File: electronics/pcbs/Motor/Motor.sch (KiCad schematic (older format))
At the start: 17 parts, among them J1 Left Encoder, J2 Right Encoder, J3 Battery, J4 I2C, P1 Digital, P10 CONN_01X01, P11 CONN_01X01, P12 CONN_01X01, P13 CONN_01X01, P2 Power, P3 Analog, P4 Analog, P5 PWM, P6 PWM, P7 Communication, P8 CONN_01X01, P9 CONN_01X01

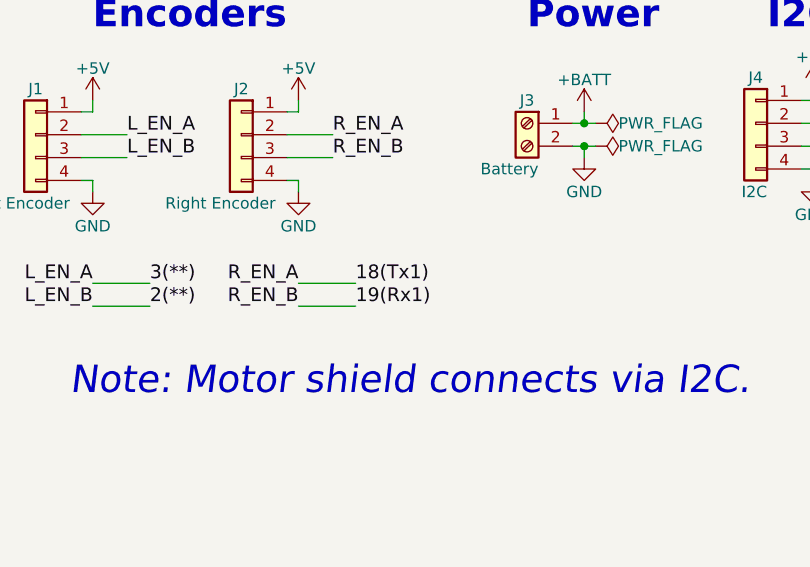
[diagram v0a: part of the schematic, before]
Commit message: Motor PCB: Redesigned PCB. Swapped pins for Encoder R's A and B so that layout was easier.
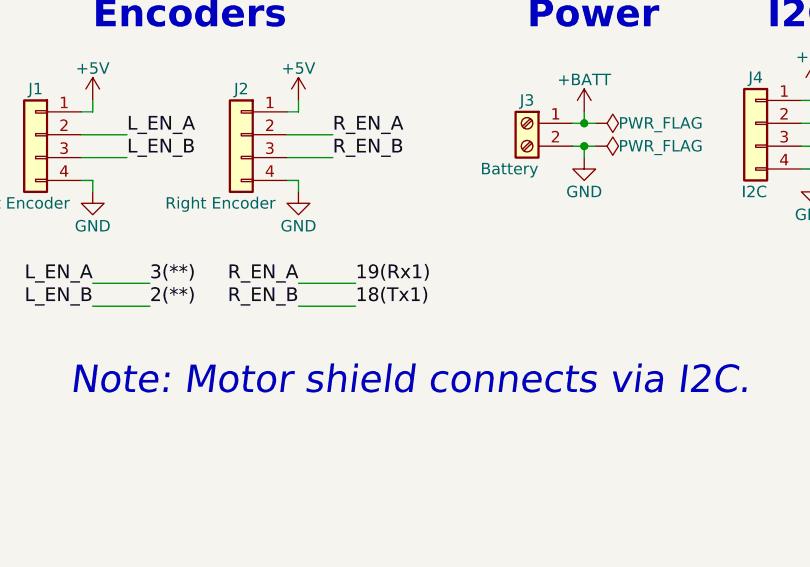
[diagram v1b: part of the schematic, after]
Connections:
- net 18(Tx1): now also J2.3 (Pin_3); no longer J2.2 (Pin_2)
- net 19(Rx1): now also J2.2 (Pin_2); no longer J2.3 (Pin_3)
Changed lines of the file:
@@
 Text Label 3950 2300 0    60   ~ 0
 3(**)
+Text Label 4850 2400 0    60   ~ 0
+18(Tx1)
 Text Label 4850 2300 0    60   ~ 0
-18(Tx1)
-Text Label 4850 2400 0    60   ~ 0
 19(Rx1)
 Wire Wire Line

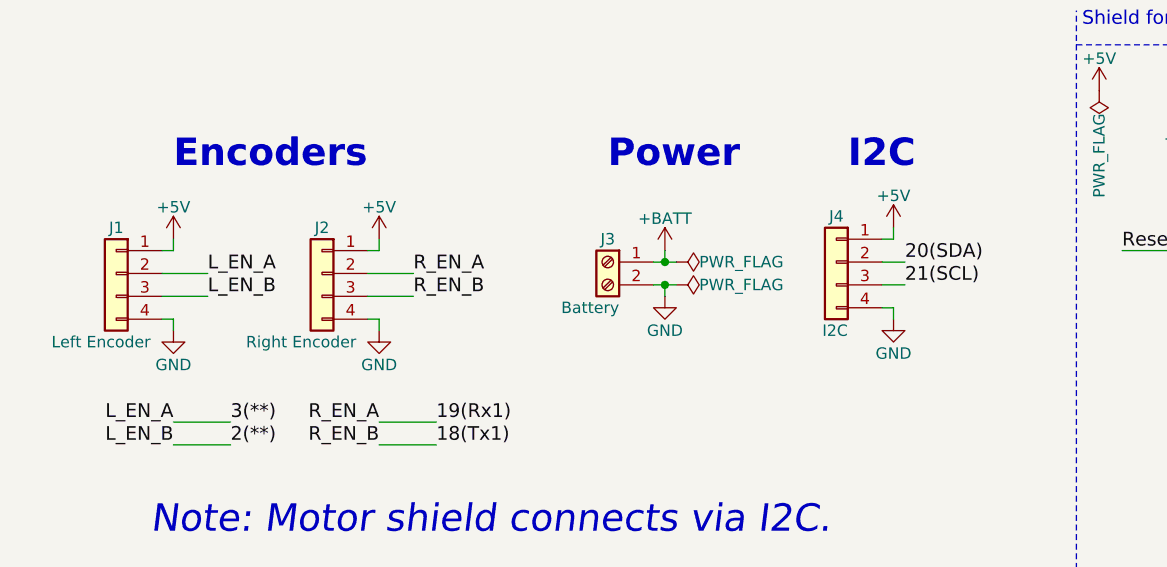
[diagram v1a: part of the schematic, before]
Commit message: Primary/Motor PCBs: Rearranged the GND pin on breakout headers so that we can avoid needing two layers. This change makes the boards more easily prototyped using hobbyist tools like the OtherMill, where plating holes and vias is difficult.
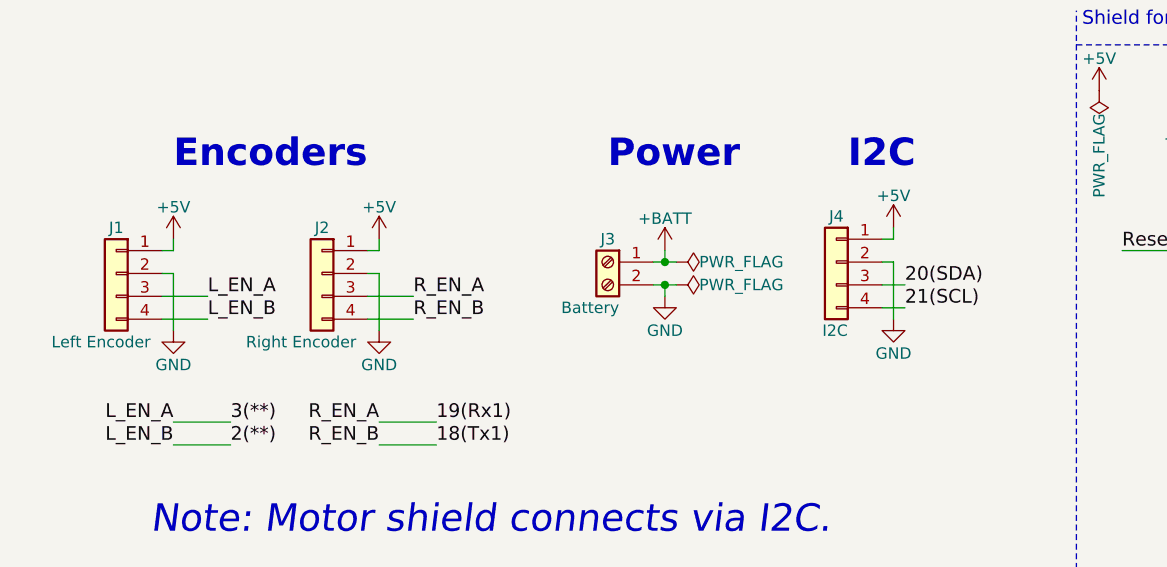
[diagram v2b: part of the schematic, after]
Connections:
- net 18(Tx1): now also J2.4 (Pin_4); no longer J2.3 (Pin_3)
- net 19(Rx1): now also J2.3 (Pin_3); no longer J2.2 (Pin_2)
- net 2(**): now also J1.4 (Pin_4); no longer J1.3 (Pin_3)
- net 20(SDA): now also J4.3 (Pin_3); no longer J4.2 (Pin_2)
- net 21(SCL): now also J4.4 (Pin_4); no longer J4.3 (Pin_3)
- net 3(**): now also J1.3 (Pin_3); no longer J1.2 (Pin_2)
- net GND: now also J1.2 (Pin_2), J2.2 (Pin_2), J4.2 (Pin_2); no longer J1.4 (Pin_4), J2.4 (Pin_4), J4.4 (Pin_4)
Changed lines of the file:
@@
 	3700 1550 3650 1550
 Wire Wire Line
-	3650 1850 3700 1850
-Wire Wire Line
-	3700 1850 3700 1900
-Wire Wire Line
-	3650 1650 3850 1650
-Wire Wire Line
-	3650 1750 3850 1750
-Text Label 3850 1650 0    60   ~ 0
+	3700 1650 3700 1900
+Text Label 3850 1750 0    60   ~ 0
 L_EN_A
-Text Label 3850 1750 0    60   ~ 0
+Text Label 3850 1850 0    60   ~ 0
 L_EN_B
 $Comp
@@
 	4600 1550 4550 1550
 Wire Wire Line
-	4550 1850 4600 1850
-Wire Wire Line
-	4600 1850 4600 1900
-Wire Wire Line
-	4550 1650 4750 1650
-Wire Wire Line
-	4550 1750 4750 1750
-Text Label 4750 1650 0    60   ~ 0
+	4600 1650 4600 1900
+Text Label 4750 1750 0    60   ~ 0
 R_EN_A
-Text Label 4750 1750 0    60   ~ 0
+Text Label 4750 1850 0    60   ~ 0
 R_EN_B
 Text Notes 3700 1200 0    120  ~ 24
@@
 Wire Wire Line
 	6850 1500 6800 1500
-$Comp
-L GND #PWR019
-U 1 1 5AB34935
-P 6850 1850
-F 0 "#PWR019" H 6850 1600 50  0001 C CNN
-F 1 "GND" H 6850 1700 50  0000 C CNN
-F 2 "" H 6850 1850 50  0000 C CNN
-F 3 "" H 6850 1850 50  0000 C CNN
-	1    6850 1850
-	1    0    0    -1
-$EndComp
-Wire Wire Line
-	6800 1800 6850 1800
-Wire Wire Line
-	6850 1800 6850 1850
-Wire Wire Line
-	6800 1600 6900 1600
-Wire Wire Line
-	6800 1700 6900 1700
-Text Label 6900 1600 0    60   ~ 0
+Wire Wire Line
+	6850 1600 6850 1850
+Text Label 6900 1700 0    60   ~ 0
 20(SDA)
-Text Label 6900 1700 0    60   ~ 0
+Text Label 6900 1800 0    60   ~ 0
 21(SCL)
 Text Label 3700 2300 2    60   ~ 0
@@
 +3.3V
 NoConn ~ 8650 1650
+Wire Wire Line
+	3650 1650 3700 1650
+Wire Wire Line
+	3650 1750 3850 1750
+Wire Wire Line
+	3850 1850 3650 1850
+Wire Wire Line
+	4550 1650 4600 1650
+Wire Wire Line
+	4550 1750 4750 1750
+Wire Wire Line
+	4750 1850 4550 1850
+$Comp
+L GND #PWR019
+U 1 1 5AB34935
+P 6850 1850
+F 0 "#PWR019" H 6850 1600 50  0001 C CNN
+F 1 "GND" H 6850 1700 50  0000 C CNN
+F 2 "" H 6850 1850 50  0000 C CNN
+F 3 "" H 6850 1850 50  0000 C CNN
+	1    6850 1850
+	1    0    0    -1
+$EndComp
+Wire Wire Line
+	6850 1600 6800 1600
+Wire Wire Line
+	6800 1700 6900 1700
+Wire Wire Line
+	6900 1800 6800 1800
 $EndSCHEMATC
